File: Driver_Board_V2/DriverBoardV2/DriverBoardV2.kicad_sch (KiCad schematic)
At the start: 29 parts, among them IC1 L7805ABV, J1 ESC1_PWR, J10 M1_OUT, J2 ESC2_PWR, J3 IO_HEADER_1, J4 BATTERY, J5 M2_IN, J6 M2_OUT, J7 IO_HEADER_2, J8 EXT +5V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

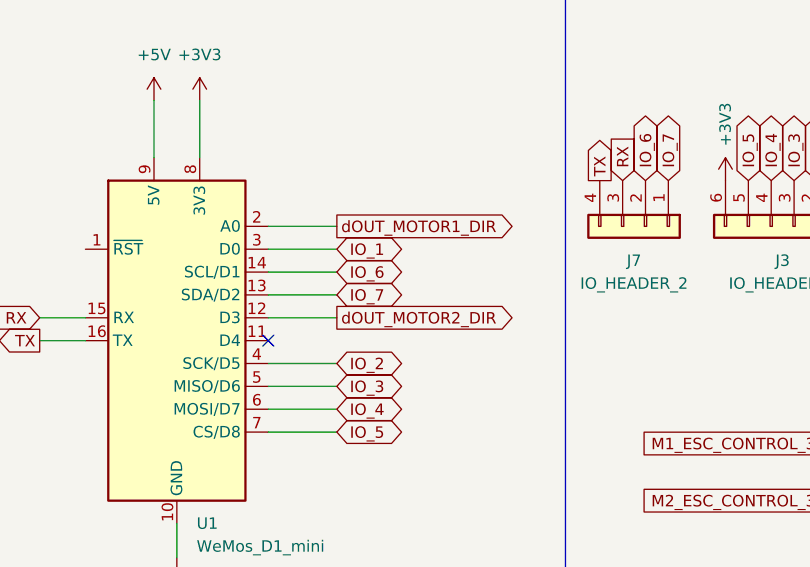
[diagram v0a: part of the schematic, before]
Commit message: Updated schematic due to layout consideration and increase 5V rail track sizes
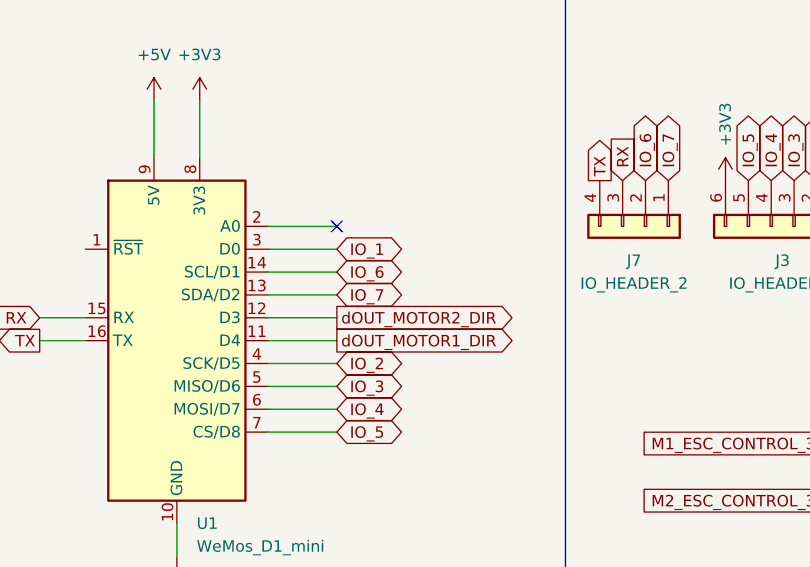
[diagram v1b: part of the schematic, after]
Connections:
- net dOUT_MOTOR1_DIR: now also U1.11 (D4); no longer U1.2 (A0)
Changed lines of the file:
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@@
 	)
 	(no_connect
-		(at 50.8 99.06)
+		(at 58.42 86.36)
 	)
 	(wire
@@
 		(pts
 			(xy 25.4 99.06) (xy 30.48 99.06)
+		)
+		(stroke
+			(width 0)
+			(type default)
+		)
+	)
+	(wire
+		(pts
+			(xy 50.8 99.06) (xy 58.42 99.06)
 		)
 		(stroke
@@
 		)
 	)
+	(global_label "dOUT_MOTOR1_DIR"
+		(shape output)
+		(at 58.42 99.06 0)
+		(fields_autoplaced yes)
+		(effects
+			(font
+				(size 1.27 1.27)
+			)
+			(justify left)
+		)
+		(property "Intersheetrefs" "${INTERSHEET_REFS}"
+			(at 78.8223 99.06 0)
+			(effects
+				(font
+					(size 1.27 1.27)
+				)
+				(justify left)
+				(hide yes)
+			)
+		)
+	)
 	(global_label "IO_1"
 		(shape bidirectional)
@@
 			(effects
 				(font
-					(size 1.27 1.27)
-				)
-				(justify left)
-				(hide yes)
-			)
-		)
-	)
-	(global_label "dOUT_MOTOR1_DIR"
-		(shape output)
-		(at 58.42 86.36 0)
-		(fields_autoplaced yes)
-		(effects
-			(font
-				(size 1.27 1.27)
-			)
-			(justify left)
-		)
-		(property "Intersheetrefs" "${INTERSHEET_REFS}"
-			(at 78.8223 86.36 0)
-			(effects
-				(font
